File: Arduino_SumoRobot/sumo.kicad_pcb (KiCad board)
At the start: 2 copper layers, 104.4 x 109.5 mm, 54 parts, among them IC1 40106D, K1 RELAY_C, K2 RELAY_C, K3 RELAY_C, K4 RELAY_C, P1 Power, P10 CONN_01X04, P11 CONN_01X04, P12 CONN_01X02, P13 CONN_01X04, P14 CONN_01X04, P15 CONN_01X04, P16 CONN_01X04, P17 CONN_01X02, P18 CONN_01X02, P2 Analog, P3 Digital, P4 Digital, P5 CONN_1, P6 CONN_1, P7 CONN_1, P8 CONN_1, P9 CONN_01X06, Q1 S8050, Q2 S8050, Q3 S8050, Q4 S8050

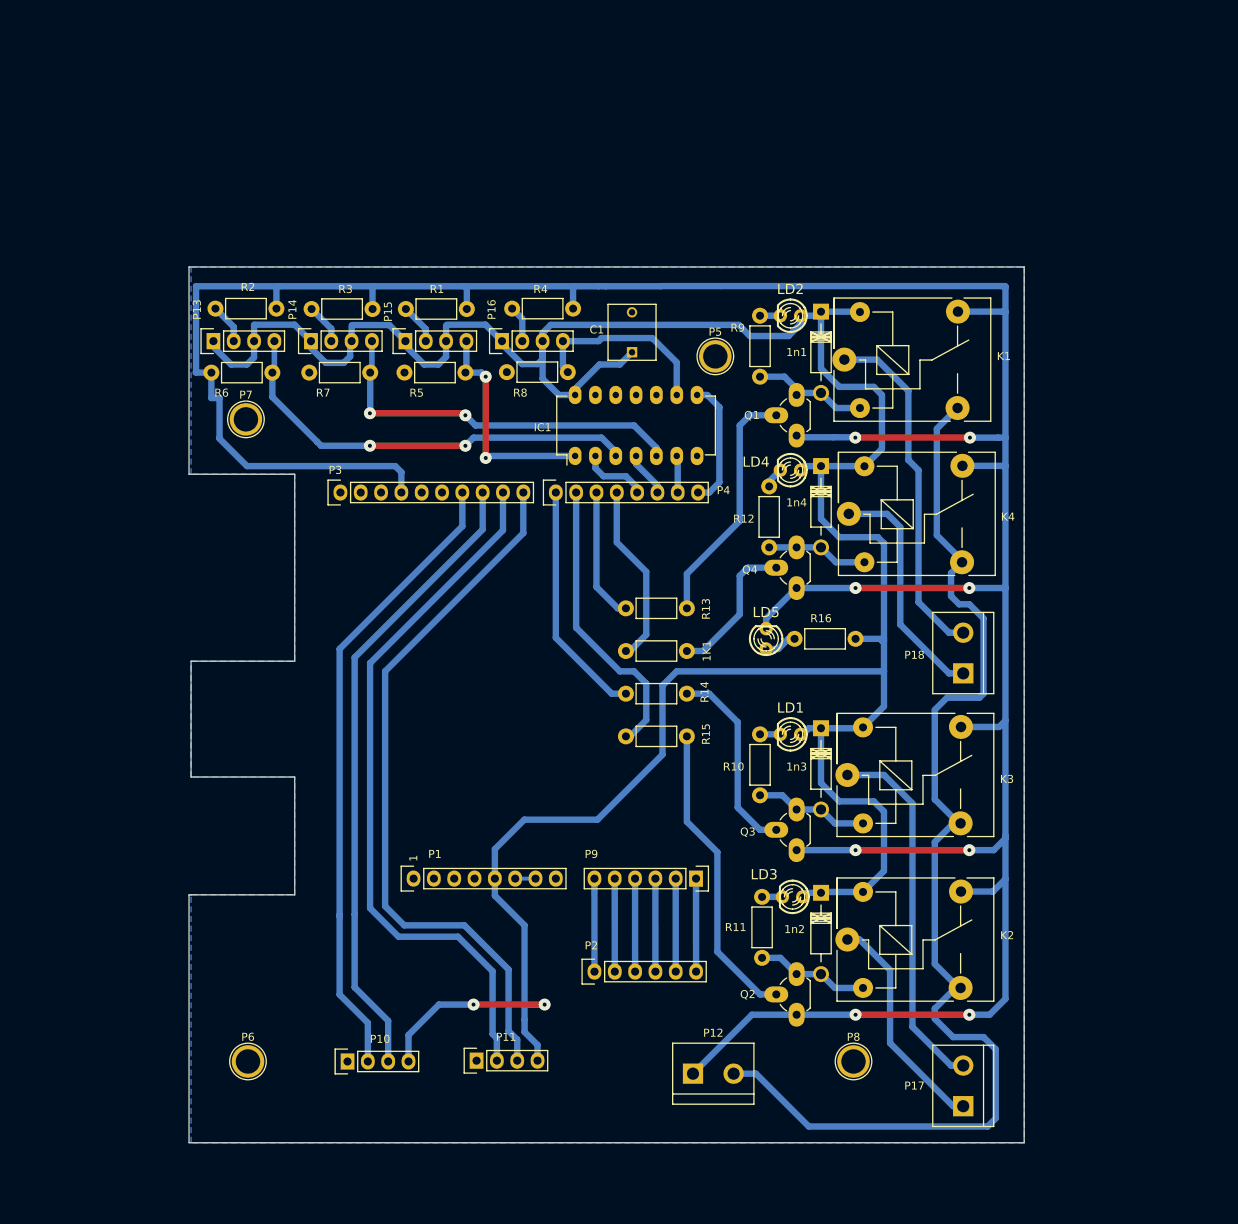
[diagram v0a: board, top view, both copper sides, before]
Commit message: Primer borrador de la versión 2 de la placa Arduino Sumo.
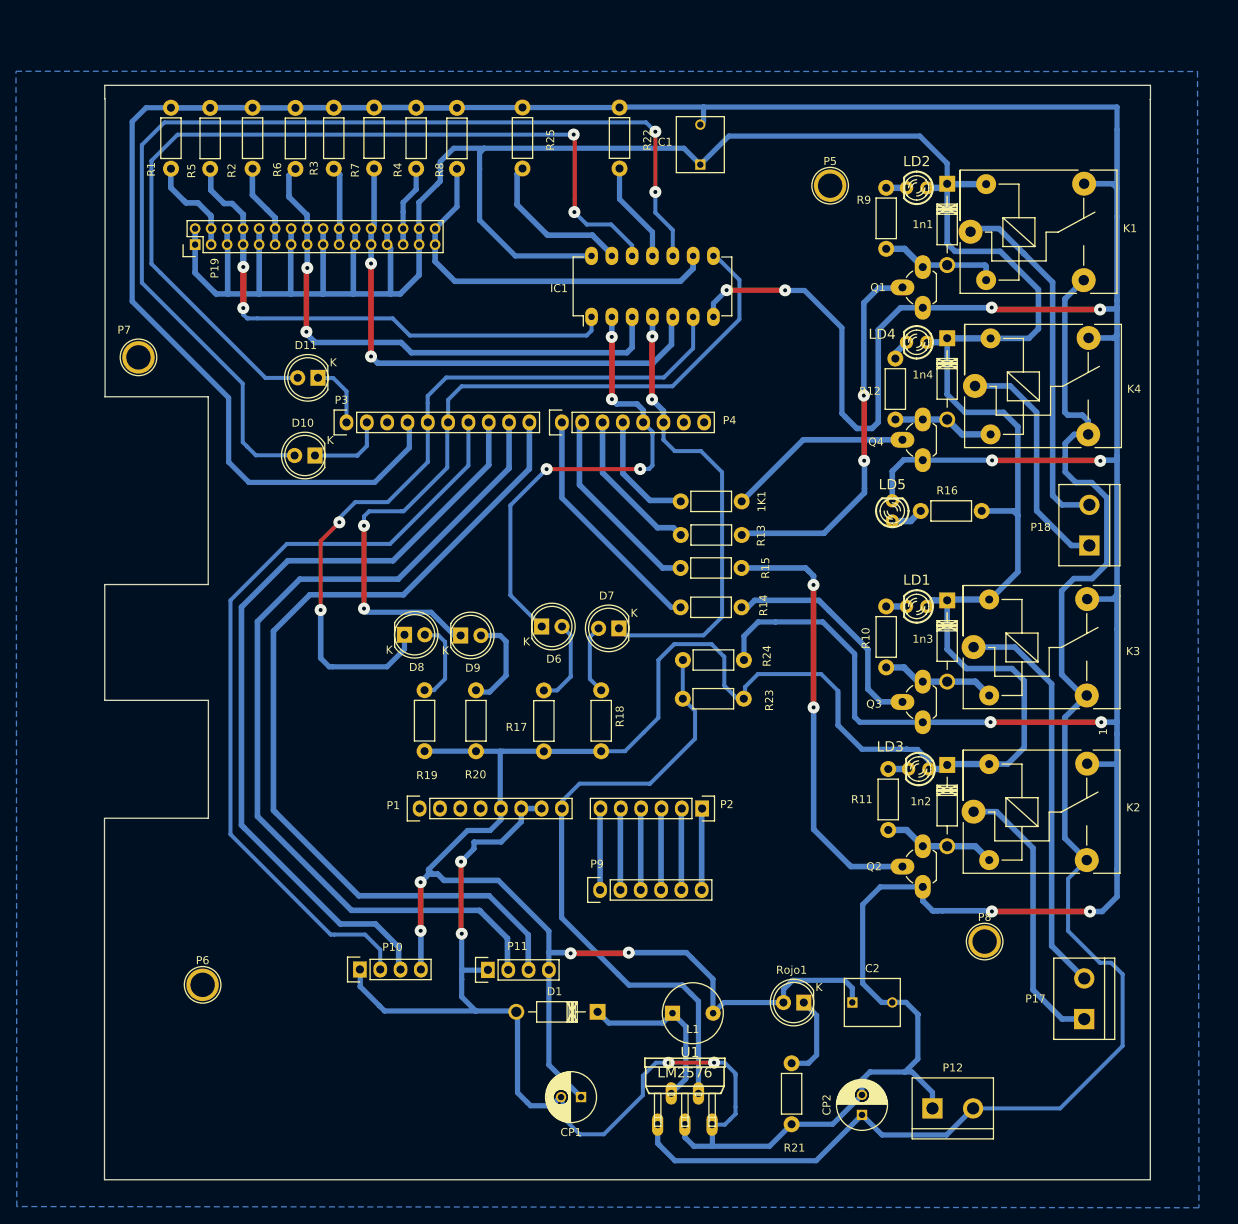
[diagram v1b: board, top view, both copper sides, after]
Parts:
- removed P13, P14, P15, P16: CONN_01X04, Pin_Headers:Pin_Header_Straight_1x04
- added C2: C, Capacitors_ThroughHole:C_Rect_L7_W6_P5, F.Cu at (193.8, 139.3)
- added CP1: CP1, Capacitors_ThroughHole:C_Radial_D6.3_L11.2_P2.5, F.Cu at (159.9, 151.1)
- added CP2: CP1, Capacitors_ThroughHole:C_Radial_D6.3_L11.2_P2.5, F.Cu at (195.0, 153.4)
- added D1: D, Diodes_ThroughHole:Diode_DO-41_SOD81_Horizontal_RM10, F.Cu at (161.9, 140.5)
- added D10: LED, LEDs:LED-5MM, F.Cu at (126.6, 70.9)
- added D11: LED, LEDs:LED-5MM, F.Cu at (127.0, 61.2)
- added D6: LED, LEDs:LED-5MM, F.Cu at (155.0, 92.3)
- added D7: LED, LEDs:LED-5MM, F.Cu at (164.6, 92.5)
- added D8: LED, LEDs:LED-5MM, F.Cu at (137.8, 93.3)
- added D9: LED, LEDs:LED-5MM, F.Cu at (144.8, 93.4)
- added L1: INDUCTOR, Inductors:INDUCTOR_V, F.Cu at (173.8, 140.7)
- added P19: CONN_02X16, Pin_Headers:Pin_Header_Straight_2x16_Pitch2.00mm, F.Cu at (111.6, 44.6)
- added R17: R, Resistors_ThroughHole:Resistor_Horizontal_RM7mm, F.Cu at (155.2, 107.9)
- added R18: R, Resistors_ThroughHole:Resistor_Horizontal_RM7mm, F.Cu at (162.4, 107.9)
- added R19: R, Resistors_ThroughHole:Resistor_Horizontal_RM7mm, F.Cu at (140.3, 107.9)
- added R20: R, Resistors_ThroughHole:Resistor_Horizontal_RM7mm, F.Cu at (146.7, 107.9)
- added R21: R, Resistors_ThroughHole:Resistor_Horizontal_RM7mm, F.Cu at (186.2, 146.9)
- added R22: R, Resistors_ThroughHole:Resistor_Horizontal_RM7mm, F.Cu at (164.7, 27.4)
- added R23: R, Resistors_ThroughHole:Resistor_Horizontal_RM7mm, F.Cu at (180.2, 101.3)
- added R24: R, Resistors_ThroughHole:Resistor_Horizontal_RM7mm, F.Cu at (172.6, 96.5)
- added R25: R, Resistors_ThroughHole:Resistor_Horizontal_RM7mm, F.Cu at (152.6, 27.4)
- added Rojo1: LED, LEDs:LED-5MM, F.Cu at (187.7, 139.3)
- added U1: LM2576, huellas:TO220-51, F.Cu at (172.8, 146.2)
- P2: renamed from P9; value CONN_01X06 -> Analog
- P9: renamed from P2; value Analog -> CONN_01X06
- moved R5 41.0 mm to (113.5, 27.5), turned to 270 degrees
- moved R6 34.7 mm to (124.2, 27.5), turned to 270 degrees
- moved R1 34.2 mm to (108.6, 35.1), turned to 90 degrees
- moved R7 34.1 mm to (134.0, 27.4), turned to 270 degrees
- moved R8 33.6 mm to (144.4, 27.5), turned to 270 degrees
- moved P12 30.3 mm to (206.3, 152.6)
- moved P5 25.7 mm to (191.0, 37.2)
- moved C1 25.0 mm to (174.8, 34.6)
- moved K1 22.5 mm to (208.6, 43.0)
- moved K2 22.5 mm to (208.9, 115.5)
- moved K3 22.5 mm to (208.9, 94.9)
- moved K4 22.5 mm to (209.1, 62.2)
- moved LD3 22.5 mm to (202.1, 110.1)
- moved R11 22.5 mm to (198.3, 110.1)
- moved R16 22.5 mm to (210.0, 77.9)
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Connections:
- IC1 pad 10: (no net) -> Net-(D10-Pad2)
- IC1 pad 11: (no net) -> Net-(IC1-Pad11)
- IC1 pad 12: (no net) -> Net-(D11-Pad2)
- IC1 pad 13: (no net) -> Net-(IC1-Pad13)
- IC1 pad 6: /1(Tx) -> Net-(D8-Pad1)
- IC1 pad 8: /0(Rx) -> Net-(D9-Pad1)
- P1 pad 1: (no net) -> Net-(P1-Pad1)
- P1 pad 2: (no net) -> Net-(P1-Pad2)
- P1 pad 3: (no net) -> Net-(P1-Pad3)
- P1 pad 4: (no net) -> Net-(P1-Pad4)
- P1 pad 8: (no net) -> /arduino
- P2 pad 1: /A5(SCL) -> /A0
- P2 pad 2: /A4(SDA) -> /A1
- P2 pad 3: /A3 -> /A2
- P2 pad 4: /A2 -> /A3
- P2 pad 5: /A1 -> /A4(SDA)
- P2 pad 6: /A0 -> /A5(SCL)
- P3 pad 1: (no net) -> Net-(D11-Pad1)
- P3 pad 2: (no net) -> Net-(D10-Pad1)
- P3 pad 3: (no net) -> Net-(P3-Pad3)
- P3 pad 5: (no net) -> Net-(D8-Pad1)
- P3 pad 6: (no net) -> Net-(D9-Pad1)
- P4 pad 7: /1(Tx) -> Net-(P4-Pad7)
- P4 pad 8: /0(Rx) -> Net-(P4-Pad8)
- P5 pad 1: (no net) -> Net-(P5-Pad1)
- P6 pad 1: (no net) -> Net-(P6-Pad1)
- P7 pad 1: (no net) -> Net-(P7-Pad1)
- P8 pad 1: (no net) -> Net-(P8-Pad1)
- P9 pad 1: /A0 -> /A5(SCL)
- P9 pad 2: /A1 -> /A4(SDA)
- P9 pad 3: /A2 -> /A3
- P9 pad 4: /A3 -> /A2
- P9 pad 5: /A4(SDA) -> /A1
- P9 pad 6: /A5(SCL) -> /A0
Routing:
- net GND: track 408.6 -> 713.8 mm, vias 8 -> 15
- net +5V: track 366.4 -> 547.3 mm, vias 2 -> 4
- net Net-(D10-Pad2): track 0.00 -> 131.8 mm, vias 0 -> 2
- net Net-(D11-Pad2): track 0.00 -> 111.2 mm, vias 0 -> 2
- net Net-(D9-Pad1): track 0.00 -> 96.6 mm, vias 0 -> 2
- net Net-(D8-Pad1): track 0.00 -> 93.9 mm, vias 0 -> 2
- net /arduino: track 0.00 -> 78.0 mm
- net /2: track 6.22 -> 57.3 mm, vias 0 -> 2
- net /3(**): track 8.37 -> 58.8 mm, vias 0 -> 4
- net +12V: track 146.9 -> 186.2 mm
- net Net-(IC1-Pad1): track 28.5 -> 67.2 mm
- net Net-(IC1-Pad9): track 23.8 -> 48.2 mm
- net /9(**): track 88.8 -> 111.0 mm
- net /8: track 89.4 -> 111.3 mm
- net Net-(D1-Pad1): track 0.00 -> 21.9 mm
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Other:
- board size 104.4 x 109.5 mm -> 130.7 x 136.8 mm

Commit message: Cambios significativos en el PCB arduino sumo. desruteo. reorganización de componentes. reglas de diseño.
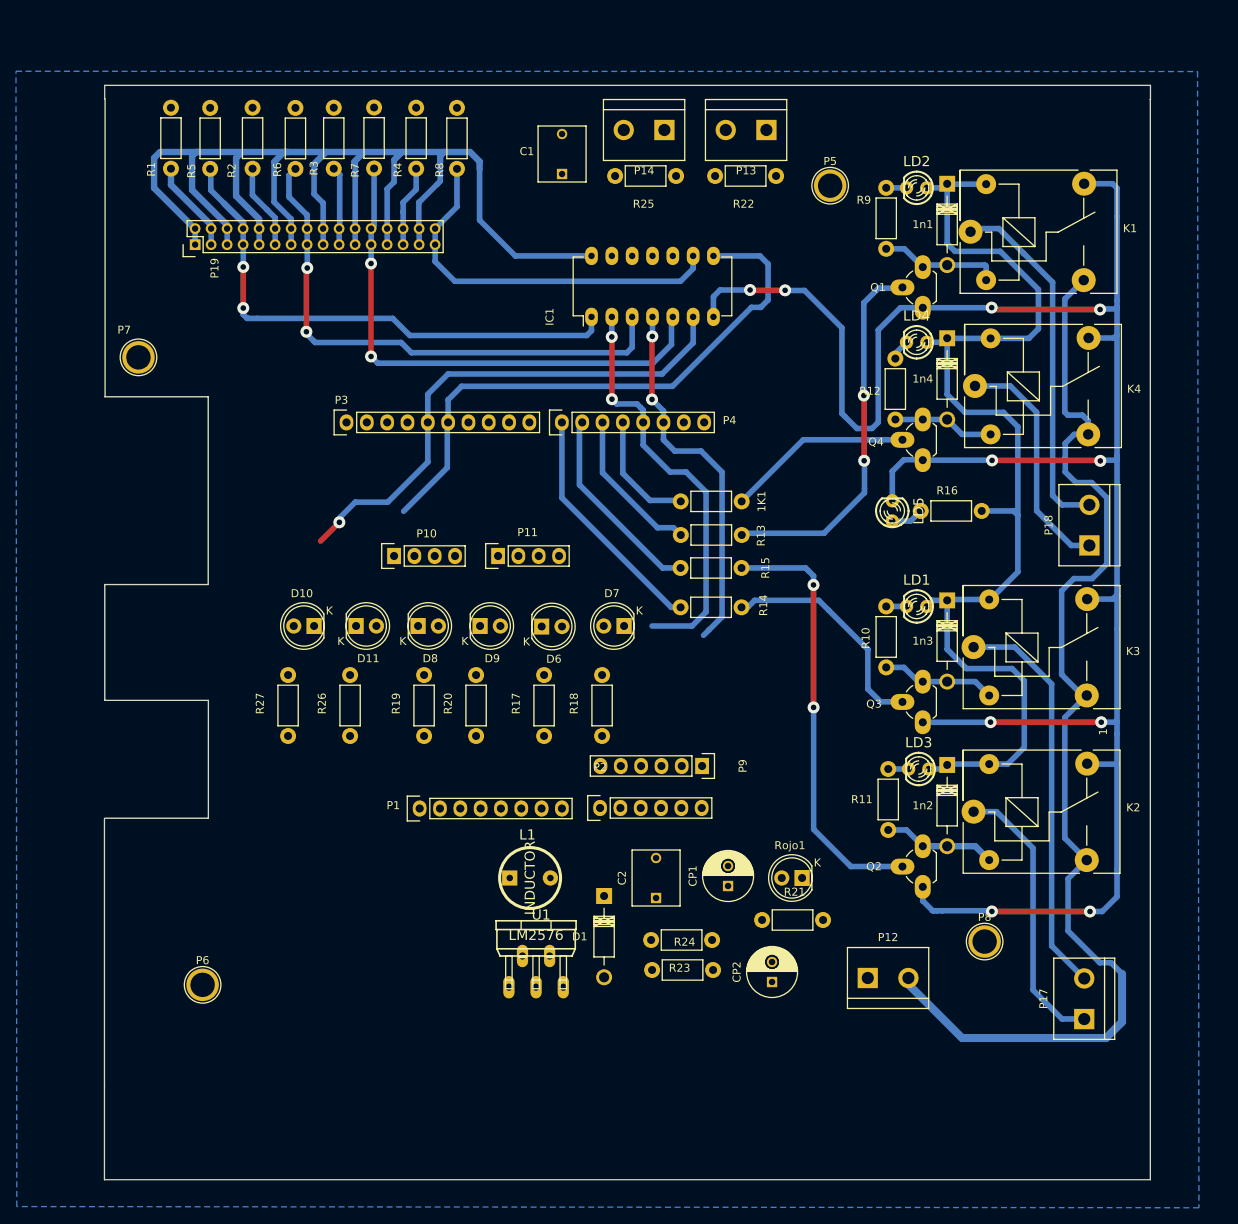
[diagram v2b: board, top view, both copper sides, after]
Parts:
- added P13: CONN_01X02, huellas:bornier2, F.Cu at (180.5, 30.2)
- added P14: CONN_01X02, huellas:bornier2, F.Cu at (167.8, 30.2)
- added R26: R, huellas:Resistor_Horizontal_RM7mm, F.Cu at (131.0, 106.0)
- added R27: R, huellas:Resistor_Horizontal_RM7mm, F.Cu at (123.2, 106.0)
- 1n1, 1n2, 1n3, 1n4, D1: footprint Diodes_ThroughHole:Diode_DO-41_SOD81_Horizontal_RM10 -> huellas:Diode_DO-41_SOD81_Horizontal_RM10
- C2: footprint Capacitors_ThroughHole:C_Rect_L7_W6_P5 -> huellas:C_Rect_L7_W6_P5
- CP1, CP2: footprint Capacitors_ThroughHole:C_Radial_D6.3_L11.2_P2.5 -> huellas:C_Radial_D6.3_L11.2_P2.5
- D10, D11, D6, D7, D8, D9, Rojo1: footprint LEDs:LED-5MM -> huellas:LED-5MM
- IC1: footprint Housings_DIP:DIP-14_W7.62mm_LongPads -> huellas:DIP-14_W7.62mm_LongPads
- L1: footprint Inductors:INDUCTOR_V -> huellas:INDUCTOR_V
- LD1, LD2, LD3, LD4, LD5: footprint Led:led-LED3MM -> huellas:led-LED3MM
- P12: value CONN_01X02 -> CONN_BATERIA12V; footprint Connect:bornier2 -> huellas:bornier2
- P17, P18: footprint Connect:bornier2 -> huellas:bornier2
- P19: footprint Pin_Headers:Pin_Header_Straight_2x16_Pitch2.00mm -> huellas:Pin_Header_Straight_2x16_Pitch2.00mm
- P2: footprint huellas:Pin_Header_Straight_1x06 -> huellas:Socket_Strip_Arduino_1x06
- P9: footprint huellas:Socket_Strip_Arduino_1x06 -> huellas:Pin_Header_Straight_1x06
- R17, R18, R19, R20, R21, R22, R23, R24, R25: footprint Resistors_ThroughHole:Resistor_Horizontal_RM7mm -> huellas:Resistor_Horizontal_RM7mm
- moved P10 51.9 mm to (136.5, 83.5)
- moved P11 51.8 mm to (149.5, 83.5)
- moved R24 38.9 mm to (168.8, 135.2)
- moved CP1 32.2 mm to (178.2, 124.8), turned to 90 degrees
- moved D11 31.4 mm to (131.8, 92.2), turned to 0 degrees
- moved R23 30.4 mm to (176.2, 131.5)
- moved C2 27.8 mm to (169.2, 126.2), turned to 90 degrees
- moved L1 26.4 mm to (153.5, 123.8)
- moved U1 25.3 mm to (154.2, 129.0)
- moved R22 21.4 mm to (184.2, 36.0), turned to 180 degrees
- moved D10 21.3 mm to (126.5, 92.2)
- moved R25 21.0 mm to (171.8, 36.0), turned to 180 degrees
- moved P9 20.1 mm to (175.0, 109.8), turned to 270 degrees
- moved CP2 20.1 mm to (183.8, 136.8)
- moved R21 18.3 mm to (182.5, 129.0), turned to 0 degrees
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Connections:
- net Net-(IC1-Pad1) renamed /pa1
- net Net-(IC1-Pad3) renamed /pa2
- net Net-(IC1-Pad5) renamed /pa3
- net Net-(IC1-Pad9) renamed /pa4
- net Net-(P19-Pad11) renamed /pr2
- net Net-(P19-Pad19) renamed /pr3
- net Net-(P19-Pad27) renamed /pr4
- net Net-(P19-Pad3) renamed /pr1
- C2 pad 1: +5V -> VCC
- CP1 pad 1: +5V -> VCC
- IC1 pad 10: Net-(D10-Pad2) -> Net-(D11-Pad1)
- IC1 pad 12: Net-(D11-Pad2) -> Net-(D10-Pad1)
- L1 pad 2: +5V -> VCC
- P1 pad 1: Net-(P1-Pad1) -> (no net)
- P1 pad 2: Net-(P1-Pad2) -> (no net)
- P1 pad 3: Net-(P1-Pad3) -> (no net)
- P1 pad 4: Net-(P1-Pad4) -> (no net)
- P1 pad 8: /arduino -> VCC
- P3 pad 1: Net-(D11-Pad1) -> Net-(D10-Pad1)
- P3 pad 2: Net-(D10-Pad1) -> Net-(D11-Pad1)
- P3 pad 3: Net-(P3-Pad3) -> (no net)
- P4 pad 7: Net-(P4-Pad7) -> (no net)
- P4 pad 8: Net-(P4-Pad8) -> (no net)
- P5 pad 1: Net-(P5-Pad1) -> (no net)
- P6 pad 1: Net-(P6-Pad1) -> (no net)
- P7 pad 1: Net-(P7-Pad1) -> (no net)
- P8 pad 1: Net-(P8-Pad1) -> (no net)
- R22 pad 1: GND -> +5V
- R23 pad 1: +5V -> VCC
- R23 pad 2: /arduino -> Net-(R23-Pad2)
- R24 pad 1: /arduino -> Net-(R23-Pad2)
- R25 pad 1: GND -> +5V
- Rojo1 pad 2: +5V -> VCC
- U1 pad 4: /arduino -> Net-(R23-Pad2)
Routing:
- net GND: track 713.8 -> 270.5 mm, vias 15 -> 11
- net +5V: track 547.3 -> 310.3 mm, vias 4 -> 0
- net Net-(D10-Pad2): track 131.8 -> 0.00 mm, vias 2 -> 0
- net /8: track 111.3 -> 0.00 mm
- net Net-(D11-Pad2): track 111.2 -> 0.00 mm, vias 2 -> 0
- net /9(**): track 111.0 -> 0.00 mm
- net /10(**/SS): track 99.7 -> 0.00 mm
- net /11(**/MOSI): track 98.5 -> 0.00 mm
- net /arduino: track 78.0 -> 0.00 mm
- net +12V: track 186.2 -> 145.0 mm
- net Net-(D8-Pad1): track 93.9 -> 65.4 mm, vias 2 -> 1
- net Net-(D9-Pad1): track 96.6 -> 73.4 mm, vias 2 -> 0
- net Net-(D1-Pad1): track 21.9 -> 0.00 mm
- net Net-(IC1-Pad13): track 19.4 -> 0.16 mm
- net Net-(IC1-Pad11): track 12.6 -> 0.00 mm
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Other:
- net class Default: trace_width 0.25 -> 0.7; via_dia 0.6 -> 1.5; via_drill 0.4 -> 0.7
- rule trace_min: 0.2 -> 0.7
- rule via_min_drill: 0.3 -> 0.7
- rule via_min_size: 0.4 -> 1.5
- board text added: "EL BORDE DE IMPRESO NO CIERRA BIEN. ELEGIR GLRILLA 1MM Y REDIBUJAR BORDE."
- board text added: "GND SE RUTEA AL FINAL"
- board text added: "HASTA ACA HACER EL PCB"
- board text added: "RUTEAR OTRA VEZ LA FUENTE INTENTAR RESPETAR LA UBICACION PROPUESTA (MOVIMIENTOS MINIMOS)"
